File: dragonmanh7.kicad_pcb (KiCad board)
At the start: 4 copper layers, 135.6 x 54.6 mm, 149 parts, among them J1 USB_C, J10 Conn_02x12_Odd_Even, J11 Conn_02x05_Odd_Even, J12 VBAT+, J13 Conn_02x05_Odd_Even, J14 VBATG, J15 Conn_02x02_Odd_Even, J16 Conn_02x02_Odd_Even, J18 Conn_02x05_Odd_Even, J2 73725-0110BLF, J3 RJ45_Amphenol_RJMG1BD3B8K1ANR, J4 105162-0001, J5 Screw_Terminal_01x06, J6 Conn_02x12_Odd_Even, J7 USB_C, J8 Screw_Terminal_01x02, J9 Conn_02x12_Odd_Even, SW1 RESET, SW2 PC13, U1 STM32H743VITx, U10 USBLC6-2SC6, U12 TCAN332, U13 ISL83483, U14 MIC2005A, U2 LAN8742A-CZ-TR, U3 AZ1117CD-3.3TRG1, U5 S25FL127SABMFI101, U6 AP63205, U7 USBLC6-2SC6, U8 STM32F042F6Px, U9 USBLC6-2SC6, Y1 8MHz, Y2 32.768KHz, Y3 25MHz

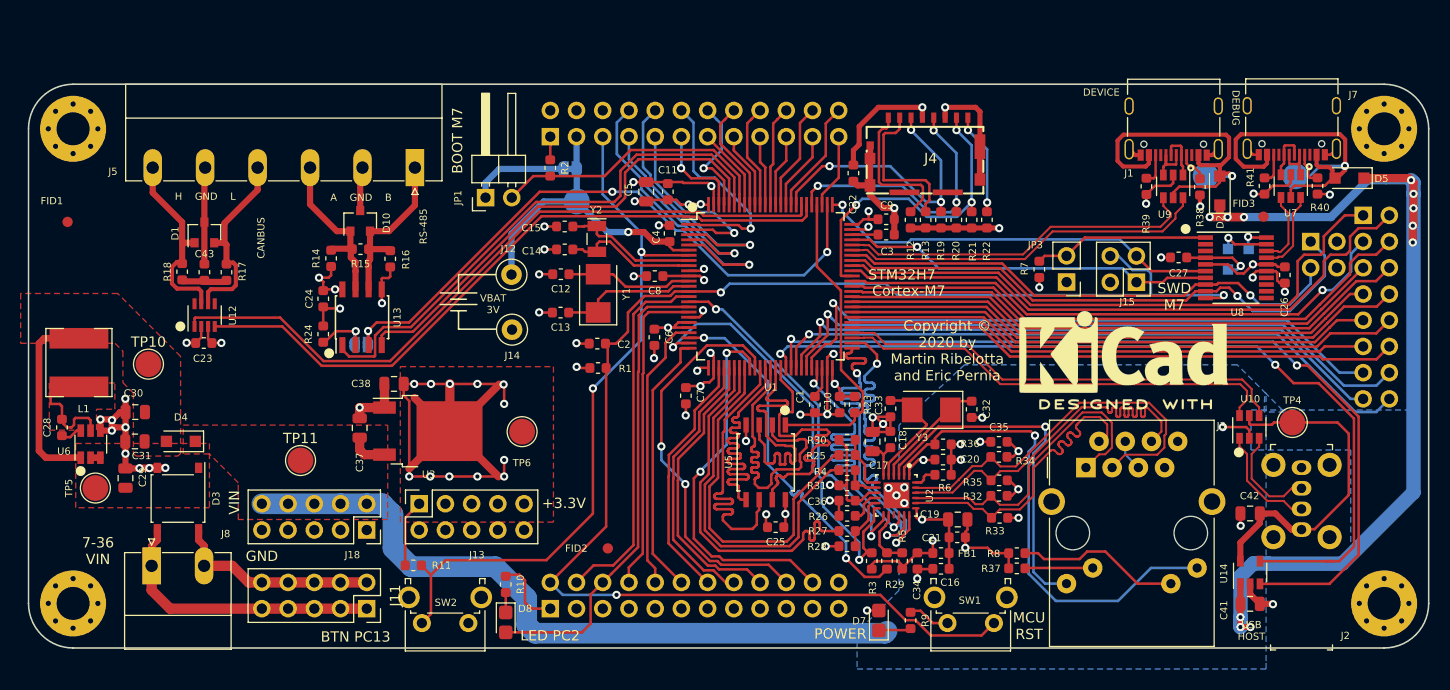
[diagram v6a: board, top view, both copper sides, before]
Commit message: Change usb-c to old usb-b connectors, move uSD to outter
Signed-off-by: Martin Ribelotta <martinribelotta@gmail.com>
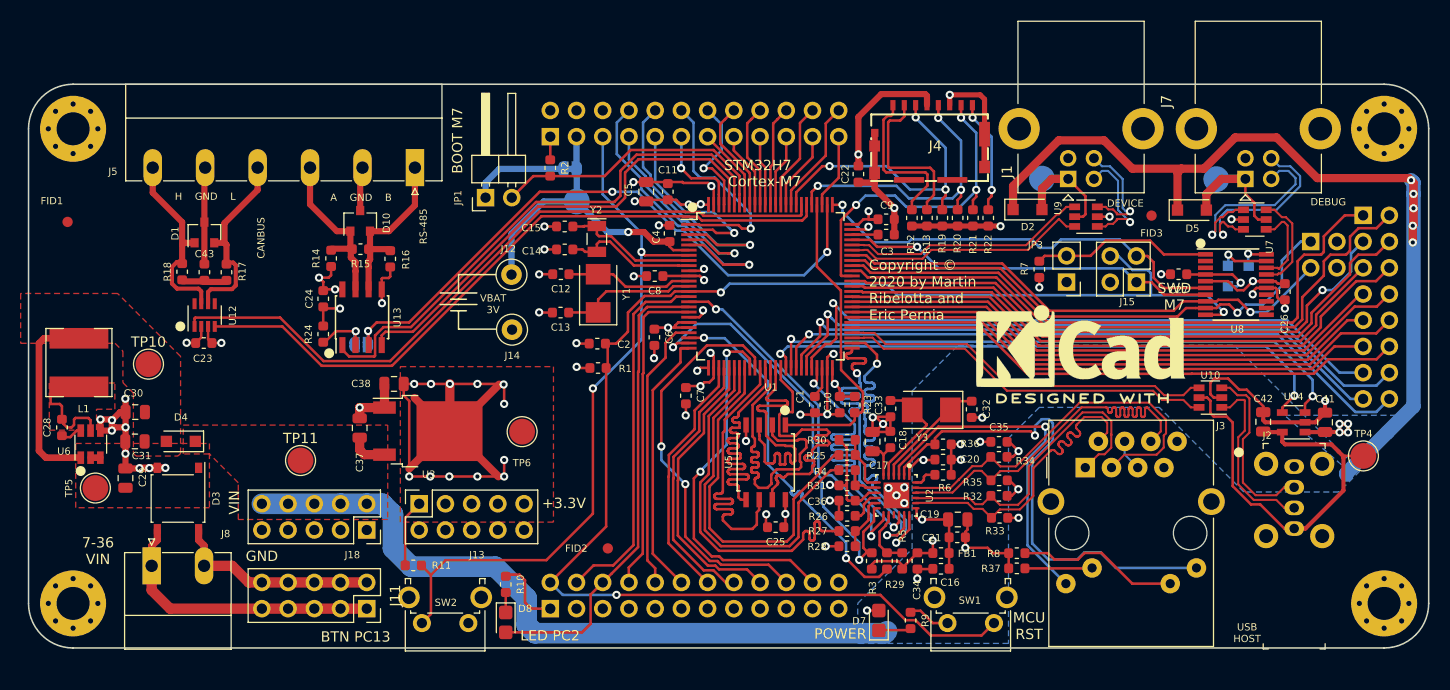
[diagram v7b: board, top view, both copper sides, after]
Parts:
- removed R38, R39, R40, R41: 5K1, Resistor_SMD:R_0603_1608Metric
- J1, J7: value USB_C -> USB_B; footprint Connector_USB:USB_C_Receptacle_Palconn_UTC16-G -> Connector_USB:USB_B_Lumberg_2411_02_Horizontal
- moved C41 19.0 mm to (184.3, 60.7), turned to 90 degrees
- moved D2 18.7 mm to (155.4, 40.1), turned to 0 degrees
- moved TP2 15.9 mm to (156.8, 37.1)
- moved D5 15.6 mm to (171.4, 40.1), turned to 0 degrees
- moved U14 15.1 mm to (181.2, 60.7), turned to 180 degrees
- moved J1 11.3 mm to (159.4, 37.1), turned to 90 degrees
- moved FID3 10.8 mm to (167.5, 40.7), turned to 0 degrees
- moved C42 8.97 mm to (178.3, 60.6), turned to 90 degrees
- moved U9 8.94 mm to (161.1, 40.8), turned to 180 degrees
- moved TP3 7.68 mm to (173.7, 37.1)
- moved TP4 7.61 mm to (188.0, 63.9)
- moved J7 6.61 mm to (176.6, 37.1), turned to 90 degrees
- moved U7 4.75 mm to (177.5, 41.0), turned to 0 degrees
- moved U10 4.72 mm to (173.2, 58.3), turned to 180 degrees
- moved LOGO1 4.22 mm to (160.6, 53.3)
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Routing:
- net /PE12: track 85.0 -> 58.4 mm
- net /PE11: track 83.4 -> 57.1 mm
- net VBUS2: track 35.7 -> 14.0 mm, vias 1 -> 0
- net VBUS1: track 34.3 -> 12.8 mm, vias 1 -> 0
- net /C_USB_SER_D-: track 4.69 -> 19.2 mm, vias 0 -> 1
- net /C_USB_SER_D+: track 4.78 -> 19.2 mm, vias 0 -> 1
- net /USBD_D-: track 35.7 -> 23.8 mm
- net /USBD_D+: track 34.9 -> 23.8 mm
- net /USBH_D+: track 43.8 -> 36.4 mm
- net /C_USBH_D+: track 10.1 -> 17.3 mm
- net /VBUS3: track 33.0 -> 39.7 mm
- net /USBH_D-: track 43.1 -> 36.4 mm
- net /C_USBH_D-: track 10.8 -> 17.3 mm
- net /C_USBD_D-: track 4.70 -> 11.2 mm, vias 0 -> 1
- net /C_USBD_D+: track 4.80 -> 10.9 mm, vias 0 -> 1
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
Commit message: Rearrange logos and vias
Signed-off-by: Martin Ribelotta <martinribelotta@gmail.com>
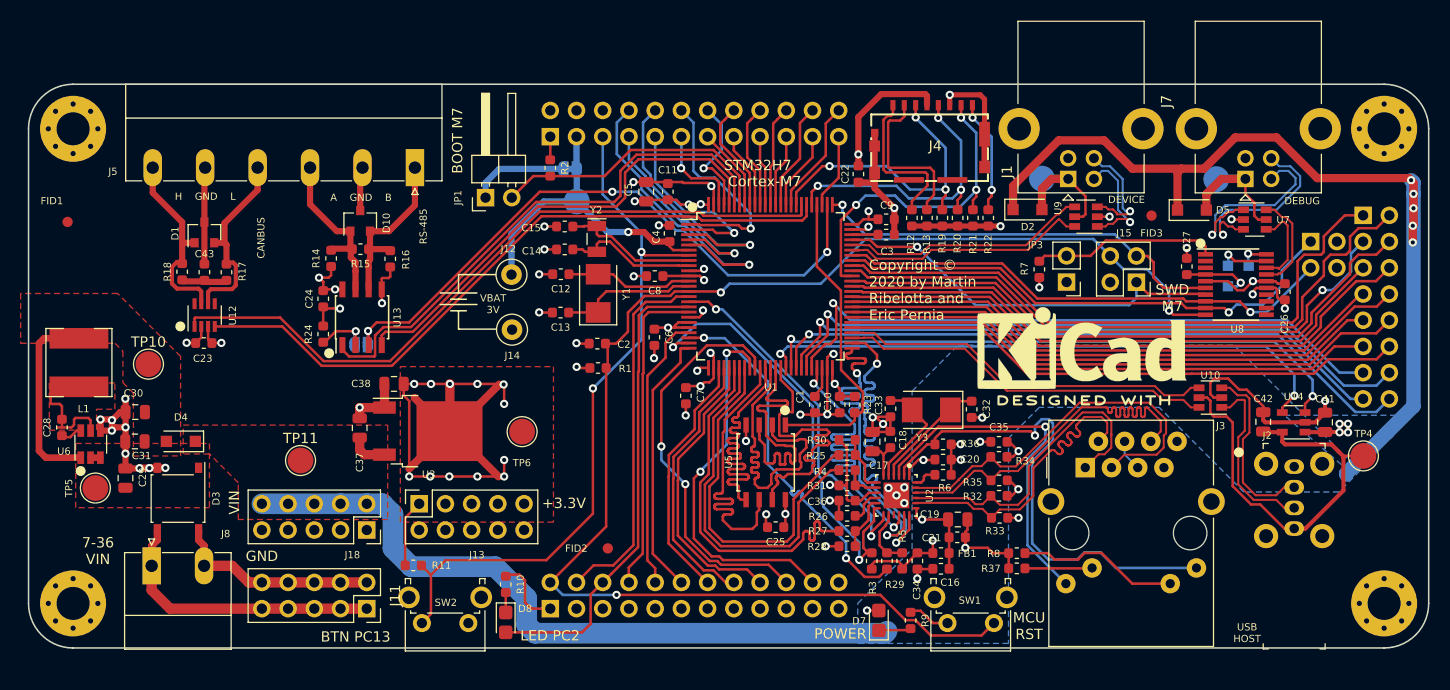
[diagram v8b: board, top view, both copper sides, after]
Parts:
- moved C27 1.09 mm to (170.9, 45.6), turned to 270 degrees
- moved LOGO1 0.23 mm to (160.7, 53.5)
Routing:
- net /~RESET: track 144.1 -> 138.5 mm
- net /SWDIO: track 36.4 -> 39.2 mm
- net /U1_TX: track 51.8 -> 50.2 mm
- net /SWCLK: track 41.7 -> 40.8 mm
- net /U1_RX: track 49.4 -> 48.5 mm
- net Net-(C28-Pad2): track 9.12 -> 9.81 mm
